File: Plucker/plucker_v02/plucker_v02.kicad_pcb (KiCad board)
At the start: 2 copper layers, 78.2 x 85.9 mm, 12 parts, among them T1 GT07-110-013

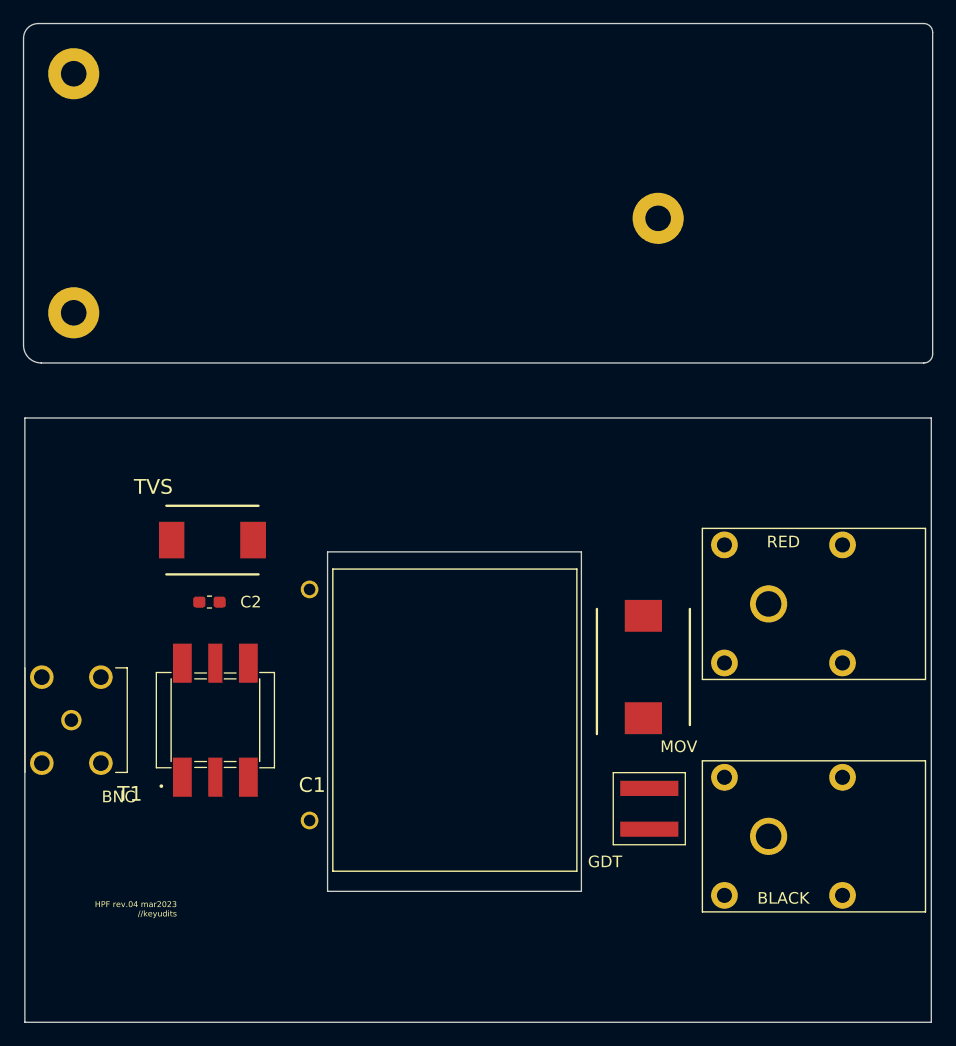
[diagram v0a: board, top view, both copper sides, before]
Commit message: Added Pulse Proof Resistor
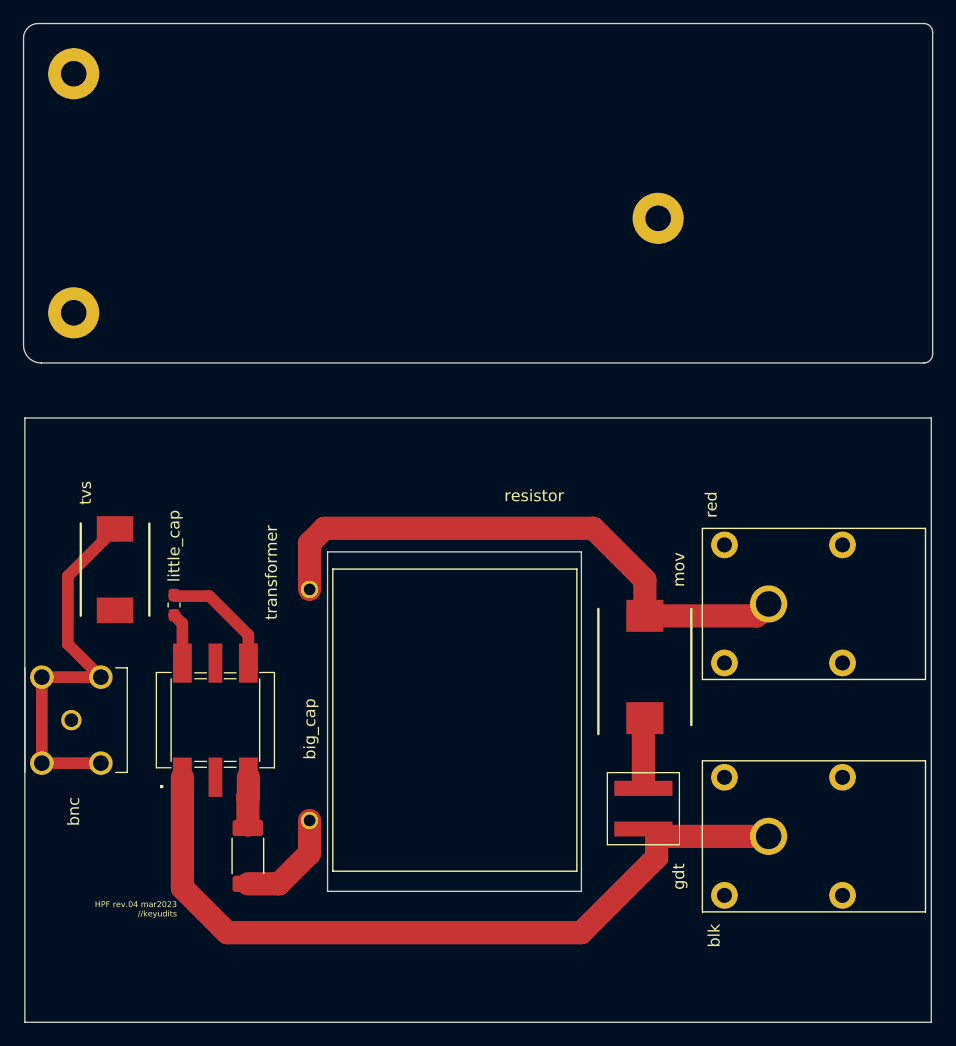
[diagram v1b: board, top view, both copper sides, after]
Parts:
- removed BLACK, RED: Conn_01x01, Banana_Jack_Safety_Right_Angle_73099:Banana_Jack_S_RA_73099
- removed BNC: BNC5-J-P-GN-RA-BH2D, BNC5-J-P-GN-RA-BH2D_kicad:BNC5JPGNRABH2D
- removed GDT: SL1002A600SP, SL1002A600SP_kicad:SL1002A600SP
- removed MOV: VP4032K122R300, VP4032K122R300_kicad:CAPPM10080X500N
- removed TVS: SMCJ5.0A, SMCJ5:DIONM7959X262N
- added D1: SMCJ918.0CA, kyuditsky_kicad:littlefuseTVS, F.Cu at (114.6, 91.9)
- added J1_BNC1: BNC5-J-P-GN-RA-BH2D, kyuditsky_kicad:BNC5JPGNRABH2D, F.Cu at (110.8, 104.9)
- added J2_BLACK1: Conn_01x01, kyuditsky_kicad:Banana_Jack_S_RA_73099, F.Cu at (170.8, 114.9)
- added J3_RED1: Conn_01x01, kyuditsky_kicad:Banana_Jack_S_RA_73099, F.Cu at (170.8, 94.9)
- added R1: 2.2, Resistor_SMD:R_2010_5025Metric_Pad1.40x2.65mm_HandSolder, F.Cu at (126.0, 116.6)
- added RV1: VP4032K122R300, kyuditsky_kicad:MOV_VP4032K122R300, F.Cu at (160.0, 100.3)
- added U1: SL1002A600SP, kyuditsky_kicad:SL1002A600SP, F.Cu at (160.0, 112.5)
- moved C2 3.06 mm to (119.6, 95.0), turned to -90 degrees
- turned T1 to 180 degrees
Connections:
- C1 pad 2: Net-(C1-Pad2) -> Net-(R1-Pad1)
- C2 pad 1: Net-(C2-Pad1) -> 0
- C2 pad 2: Net-(C2-Pad2) -> Out
- T1 pad 1: Net-(C2-Pad1) -> Net-(J2_BLACK1-Pad1)
- T1 pad 2: Net-(T1-Pad2) -> unconnected-(T1-Pad2)
- T1 pad 3: Net-(C2-Pad2) -> Net-(R2-Pad2)
- T1 pad 4: Net-(J2_BLACK1-Pad1) -> 0
- T1 pad 5: Net-(T1-Pad5) -> unconnected-(T1-Pad5)
- T1 pad 6: Net-(C1-Pad2) -> Out
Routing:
- net Net-(J2_BLACK1-Pad1): track 0.00 -> 66.1 mm
- net Net-(V1-Pad2): track 0.00 -> 49.4 mm
- net 0: track 0.00 -> 44.0 mm
- net Net-(R1-Pad1): track 0.00 -> 9.22 mm
- net Net-(RV1-Pad1): track 0.00 -> 5.53 mm
- net Out: track 0.00 -> 5.02 mm
- net Net-(R2-Pad2): track 0.00 -> 4.14 mm
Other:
- board text added: "big_cap"
- board text added: "blk"
- board text added: "bnc"
- board text added: "gdt"
- board text added: "little_cap"
- board text added: "mov"
- board text added: "red"
- board text added: "resistor"
- board text added: "transformer"
- board text added: "tvs"
